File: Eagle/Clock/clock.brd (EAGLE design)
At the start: 100 x 100 mm, 30 parts

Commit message: added gerber files for each board
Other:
- board text added: "MARIE PC Clock Architecture designed by: Dr. Linda Null Hardware implementation by: Richard Bowser"
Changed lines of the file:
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@@
 <wire x1="100" y1="100" x2="0" y2="100" width="0" layer="20"/>
 <wire x1="0" y1="100" x2="0" y2="0" width="0" layer="20"/>
+<text x="26" y="56" size="1.778" layer="26" rot="MR180">MARIE PC
+Clock
+Architecture designed by: Dr. Linda Null
+Hardware implementation by: Richard Bowser</text>
 </plain>
 <attributes>
@@
 <attribute name="POPULARITY" value="48" x="81" y="21" size="1.778" layer="27" display="off"/>
 <attribute name="SPICEPREFIX" value="R" x="81" y="21" size="1.778" layer="27" display="off"/>
-<attribute name="VALUE" x="34.1144" y="81.4774" size="0.9906" layer="27" ratio="10"/>
+<attribute name="VALUE" x="32.1144" y="81.4774" size="0.9906" layer="27" ratio="10"/>
 </element>
 <element name="R3" library="rcl" library_urn="urn:adsk.eagle:library:334" package="0204/7" package3d_urn="urn:adsk.eagle:package:23498/2" value="1k" x="77.58" y="87.96" smashed="yes">
@@
 </drawing>
 <compatibility>
+<note version="6.3" minversion="6.2.2" severity="warning">
+Since Version 6.2.2 text objects can contain more than one line,
+which will not be processed correctly with this version.
+</note>
 <note version="8.2" severity="warning">
 Since Version 8.2, EAGLE supports online libraries. The ids

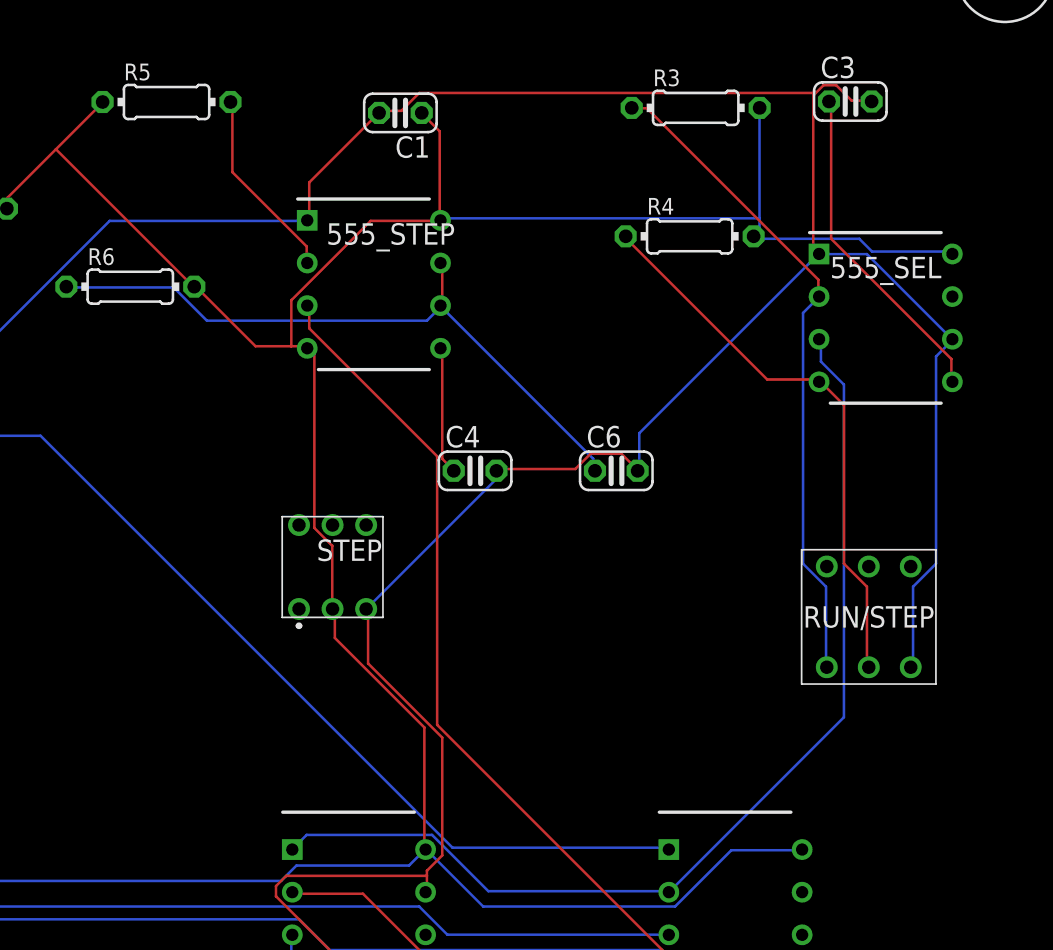
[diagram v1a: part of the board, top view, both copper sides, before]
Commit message: started adding revision 2 to fix errors in first set of boards
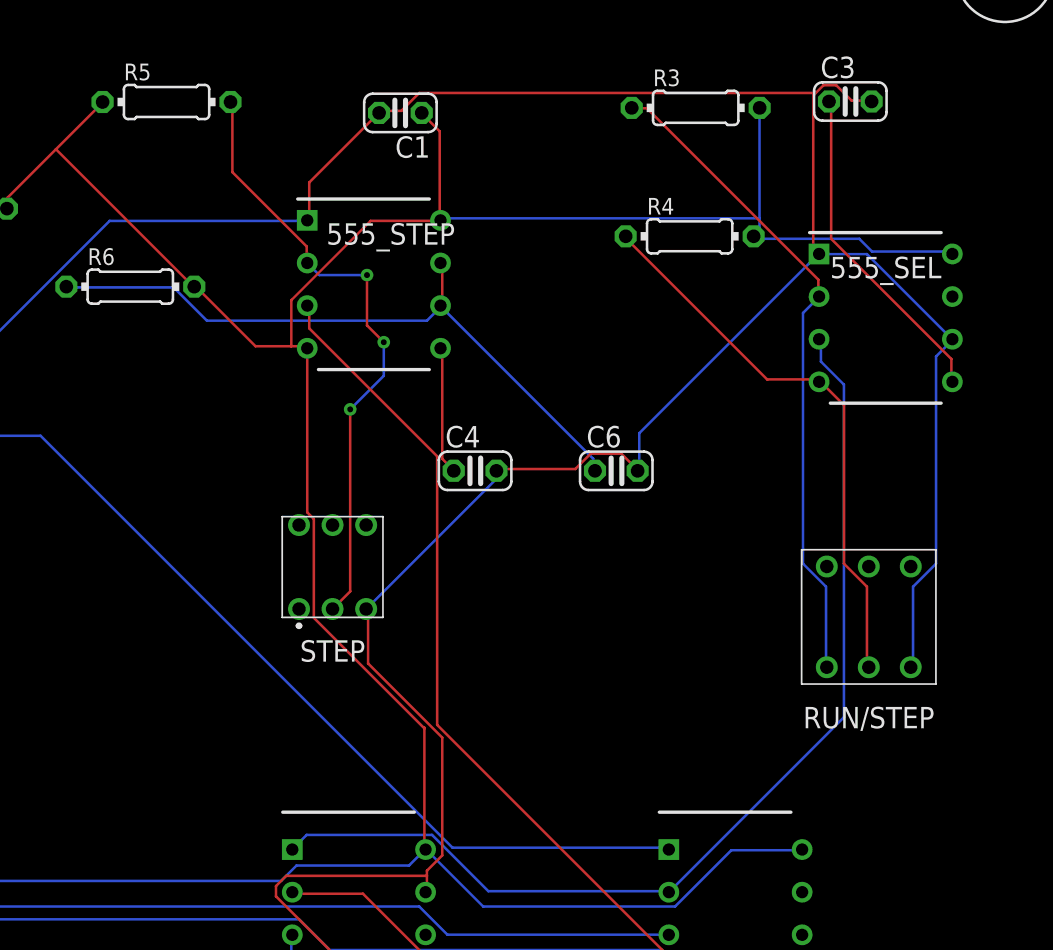
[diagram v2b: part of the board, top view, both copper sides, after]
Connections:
- net N$7: now also STEP.A2
- net VCC: no longer STEP.A2
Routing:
- net N$7: track 11.5 -> 36.8 mm, vias 0 -> 3
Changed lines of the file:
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@@
 <drawing>
 <settings>
-<setting alwaysvectorfont="yes"/>
+<setting alwaysvectorfont="no"/>
 <setting verticaltext="up"/>
 </settings>
@@
 <attribute name="MOUSER_PART_NUMBER" value="642-MHPS2285" x="140" y="14" size="1.778" layer="27" display="off"/>
 <attribute name="MOUSER_PRICE-STOCK" value="https://www.mouser.com/Search/Refine.aspx?Keyword=642-MHPS2285" x="140" y="14" size="1.778" layer="27" display="off"/>
-<attribute name="NAME" x="87.89" y="57.64" size="1.27" layer="25" align="center"/>
-<attribute name="VALUE" x="87.89" y="51.64" size="1.27" layer="27" align="center"/>
+<attribute name="NAME" x="87.89" y="51.64" size="1.27" layer="25" align="center"/>
+<attribute name="VALUE" x="87.89" y="57.64" size="1.27" layer="27" align="center"/>
 </element>
 <element name="STEP" library="SamacSys_Parts" package="MHPS2273N" value="MHPS2273N" x="55.95" y="60.61" smashed="yes">
@@
 <attribute name="MOUSER_PART_NUMBER" value="642-MHPS2273N" x="75" y="6" size="1.778" layer="27" display="off"/>
 <attribute name="MOUSER_PRICE-STOCK" value="https://www.mouser.com/Search/Refine.aspx?Keyword=642-MHPS2273N" x="75" y="6" size="1.778" layer="27" display="off"/>
-<attribute name="NAME" x="56.95" y="61.61" size="1.27" layer="25" align="center"/>
-<attribute name="VALUE" x="55.95" y="55.61" size="1.27" layer="27" align="center"/>
+<attribute name="NAME" x="55.95" y="55.61" size="1.27" layer="25" align="center"/>
+<attribute name="VALUE" x="55.95" y="60.61" size="1.27" layer="27" align="center"/>
 </element>
 <element name="U$1" library="holes" library_urn="urn:adsk.eagle:library:237" package="2,8" package3d_urn="urn:adsk.eagle:package:14271/1" value="" x="4" y="4" smashed="yes"/>
@@
 <contactref element="R6" pad="2"/>
 <contactref element="555_STEP" pad="4"/>
-<contactref element="R5" pad="1"/>
-<contactref element="STEP" pad="A2"/>
 <contactref element="555_RUN" pad="4"/>
 <contactref element="555_RUN" pad="8"/>
@@
 <wire x1="39.4716" y1="85.4964" x2="36.576" y2="82.6008" width="0.1524" layer="1"/>
 <wire x1="36.576" y1="81.9912" x2="36.55" y2="81.96" width="0.1524" layer="1"/>
-<wire x1="42.2148" y1="88.2396" x2="42.25" y2="88.31" width="0.1524" layer="1"/>
 <wire x1="62.3316" y1="86.5632" x2="62.3316" y2="81.3816" width="0.1524" layer="1"/>
 <wire x1="61.2648" y1="87.63" x2="62.3316" y2="86.5632" width="0.1524" layer="1"/>
@@
 <wire x1="54.4068" y1="73.7616" x2="54.44" y2="73.64" width="0.1524" layer="1"/>
 <wire x1="47.8536" y1="77.2668" x2="47.71" y2="77.31" width="0.1524" layer="1"/>
-<wire x1="55.9308" y1="61.8744" x2="55.9308" y2="58.2168" width="0.1524" layer="1"/>
-<wire x1="54.864" y1="62.9412" x2="55.9308" y2="61.8744" width="0.1524" layer="1"/>
-<wire x1="54.864" y1="73.3044" x2="54.864" y2="62.9412" width="0.1524" layer="1"/>
 <wire x1="54.5592" y1="73.6092" x2="54.864" y2="73.3044" width="0.1524" layer="1"/>
-<wire x1="55.9308" y1="58.2168" x2="55.95" y2="58.11" width="0.1524" layer="1"/>
 <wire x1="54.5592" y1="73.6092" x2="54.44" y2="73.64" width="0.1524" layer="1"/>
 <wire x1="58.2168" y1="81.2292" x2="62.3316" y2="81.2292" width="0.1524" layer="1"/>
@@
 <wire x1="22.098" y1="79.5528" x2="22.09" y2="79.48" width="0.1524" layer="16"/>
 <wire x1="36.4236" y1="81.8388" x2="36.55" y2="81.96" width="0.1524" layer="16"/>
-<wire x1="61.4172" y1="51.054" x2="61.4172" y2="43.8912" width="0.1524" layer="1"/>
-<wire x1="56.0832" y1="56.388" x2="61.4172" y2="51.054" width="0.1524" layer="1"/>
-<wire x1="56.0832" y1="58.0644" x2="56.0832" y2="56.388" width="0.1524" layer="1"/>
+<wire x1="61.4172" y1="51.054" x2="61.4172" y2="51" width="0.1524" layer="1"/>
+<wire x1="61.4172" y1="51" x2="61.4172" y2="43.8912" width="0.1524" layer="1"/>
 <wire x1="61.4172" y1="43.8912" x2="61.49" y2="43.78" width="0.1524" layer="1"/>
-<wire x1="56.0832" y1="58.0644" x2="55.95" y2="58.11" width="0.1524" layer="1"/>
+<contactref element="R5" pad="1"/>
+<wire x1="54.44" y1="73.64" x2="54.44" y2="63.8681875" width="0.1524" layer="1"/>
+<wire x1="54.44" y1="63.8681875" x2="54.8326" y2="63.4755875" width="0.1524" layer="1"/>
+<wire x1="54.8326" y1="57.5846" x2="61.4172" y2="51" width="0.1524" layer="1"/>
+<wire x1="54.8326" y1="63.4755875" x2="54.8326" y2="57.5846" width="0.1524" layer="1"/>
+<wire x1="42.2148" y1="88.2396" x2="42.25" y2="88.31" width="0" layer="19" extent="1-1"/>
 </signal>
 <signal name="N$1">
@@
 <wire x1="76.0476" y1="33.6804" x2="75.98" y2="33.62" width="0.1524" layer="1"/>
 </signal>
-<signal name="N$7">
-<contactref element="555_STEP" pad="2"/>
-<contactref element="R5" pad="2"/>
-<wire x1="54.4068" y1="79.7052" x2="54.4068" y2="78.7908" width="0.1524" layer="1"/>
-<wire x1="49.9872" y1="84.1248" x2="54.4068" y2="79.7052" width="0.1524" layer="1"/>
-<wire x1="49.9872" y1="88.2396" x2="49.9872" y2="84.1248" width="0.1524" layer="1"/>
-<wire x1="54.4068" y1="78.7908" x2="54.44" y2="78.72" width="0.1524" layer="1"/>
-<wire x1="49.9872" y1="88.2396" x2="49.87" y2="88.31" width="0.1524" layer="1"/>
-</signal>
 <signal name="N$8">
 <contactref element="555_SEL" pad="2"/>
@@
 <wire x1="25.146" y1="36.7284" x2="25.12" y2="36.7" width="0.1524" layer="16"/>
 </signal>
+<signal name="N$7">
+<contactref element="STEP" pad="A2"/>
+<contactref element="555_STEP" pad="2"/>
+<wire x1="54.4068" y1="79.7052" x2="54.4068" y2="78.7908" width="0.1524" layer="1"/>
+<wire x1="49.9872" y1="84.1248" x2="54.4068" y2="79.7052" width="0.1524" layer="1"/>
+<wire x1="49.9872" y1="88.2396" x2="49.9872" y2="84.1248" width="0.1524" layer="1"/>
+<wire x1="54.4068" y1="78.7908" x2="54.44" y2="78.72" width="0.1524" layer="1"/>
+<contactref element="R5" pad="2"/>
+<wire x1="55.95" y1="58.11" x2="57" y2="59.16" width="0.1524" layer="1"/>
+<wire x1="57" y1="59.16" x2="57" y2="70" width="0.1524" layer="1"/>
+<via x="57" y="70" extent="1-16" drill="0.35"/>
+<wire x1="57" y1="70" x2="59" y2="72" width="0.1524" layer="16"/>
+<wire x1="59" y1="72" x2="59" y2="74" width="0.1524" layer="16"/>
+<via x="59" y="74" extent="1-16" drill="0.35"/>
+<wire x1="59" y1="74" x2="58" y2="75" width="0.1524" layer="1"/>
+<wire x1="58" y1="75" x2="58" y2="78" width="0.1524" layer="1"/>
+<via x="58" y="78" extent="1-16" drill="0.35"/>
+<wire x1="58" y1="78" x2="55.16" y2="78" width="0.1524" layer="16"/>
+<wire x1="55.16" y1="78" x2="54.44" y2="78.72" width="0.1524" layer="16"/>
+<wire x1="49.9872" y1="88.2396" x2="49.87" y2="88.31" width="0" layer="19" extent="1-1"/>
+</signal>
 </signals>
